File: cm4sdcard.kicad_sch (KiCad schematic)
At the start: 5 parts, among them J5 MEM2067-02-180-00-A_REVB, U9 LM3525M-H_NPOB

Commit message: respin
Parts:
- renumbered C18 to C20, C19 to C21, R24 to R27, U9 to U10
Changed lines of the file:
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@@
   (symbol (lib_id "power:GND") (at 178.435 128.27 0) (unit 1)
     (in_bom yes) (on_board yes)
-    (property "Reference" "#PWR030" (id 0) (at 178.435 134.62 0)
+    (property "Reference" "#PWR031" (id 0) (at 178.435 134.62 0)
       (effects (font (size 1.27 1.27)) hide)
     )
@@
   (symbol (lib_id "Device:R_Small") (at 104.14 66.04 90) (unit 1)
     (in_bom yes) (on_board yes) (fields_autoplaced)
-    (property "Reference" "R24" (id 0) (at 104.14 60.96 90))
+    (property "Reference" "R27" (id 0) (at 104.14 60.96 90))
     (property "Value" "12k 1%" (id 1) (at 104.14 63.5 90))
     (property "Footprint" "Resistor_SMD:R_0402_1005Metric" (id 2) (at 104.14 66.04 0)
@@
   (symbol (lib_id "Device:C_Small") (at 127 71.12 90) (unit 1)
     (in_bom yes) (on_board yes)
-    (property "Reference" "C18" (id 0) (at 125.73 69.85 90)
+    (property "Reference" "C20" (id 0) (at 125.73 69.85 90)
       (effects (font (size 1.27 1.27)) (justify left))
     )
@@
   (symbol (lib_id "power:GND") (at 167.64 83.82 0) (unit 1)
     (in_bom yes) (on_board yes)
-    (property "Reference" "#PWR029" (id 0) (at 167.64 90.17 0)
+    (property "Reference" "#PWR030" (id 0) (at 167.64 90.17 0)
       (effects (font (size 1.27 1.27)) hide)
     )
@@
   (symbol (lib_id "power:GND") (at 134.62 83.82 0) (unit 1)
     (in_bom yes) (on_board yes)
-    (property "Reference" "#PWR028" (id 0) (at 134.62 90.17 0)
+    (property "Reference" "#PWR029" (id 0) (at 134.62 90.17 0)
       (effects (font (size 1.27 1.27)) hide)
     )
@@
   (symbol (lib_id "Power_Protection_TI:LM3525M-H_NPOB") (at 144.78 68.58 0) (unit 1)
     (in_bom yes) (on_board yes)
-    (property "Reference" "U9" (id 0) (at 139.7 62.23 0))
+    (property "Reference" "U10" (id 0) (at 139.7 62.23 0))
     (property "Value" "LM3525M-H_NPOB" (id 1) (at 144.78 78.105 0))
     (property "Footprint" "Package_SO_MyOwn:SOIC-8_3.9x4.9mm_P1.27mm" (id 2) (at 145.034 86.106 0)
@@
   (symbol (lib_id "Device:C_Small") (at 167.64 68.58 0) (mirror x) (unit 1)
     (in_bom yes) (on_board yes)
-    (property "Reference" "C19" (id 0) (at 169.545 67.945 0)
+    (property "Reference" "C21" (id 0) (at 169.545 67.945 0)
       (effects (font (size 1.27 1.27)) (justify left))
     )

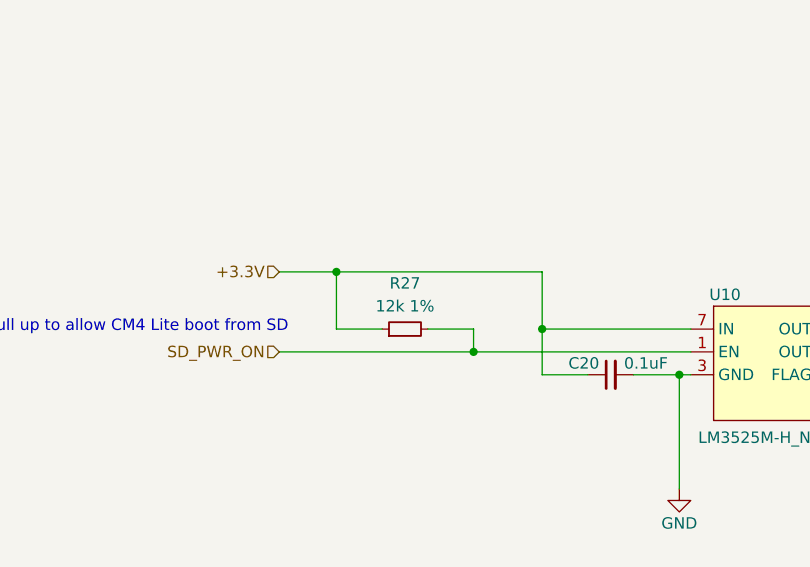
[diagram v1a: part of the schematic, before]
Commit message: fixed I2C ping indicator
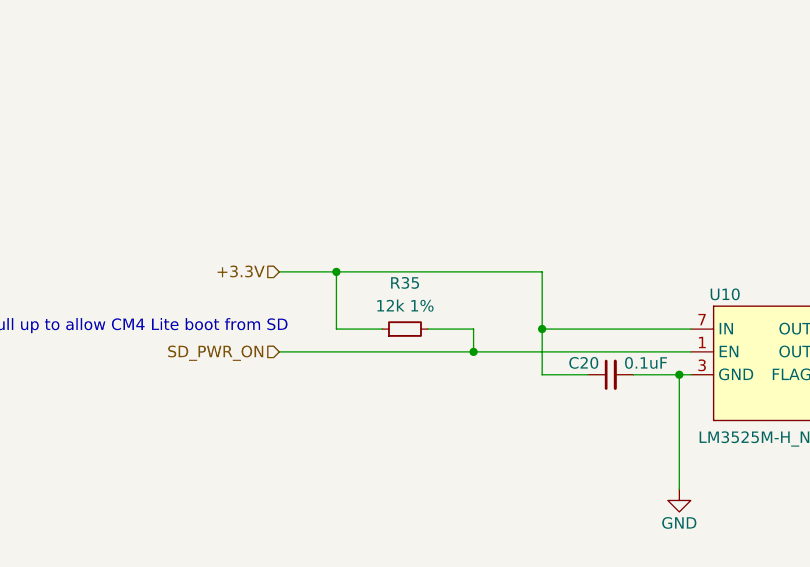
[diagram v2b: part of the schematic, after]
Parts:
- renumbered R27 to R35
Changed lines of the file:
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@@
   (symbol (lib_id "power:GND") (at 178.435 128.27 0) (unit 1)
     (in_bom yes) (on_board yes)
-    (property "Reference" "#PWR031" (id 0) (at 178.435 134.62 0)
+    (property "Reference" "#PWR033" (id 0) (at 178.435 134.62 0)
       (effects (font (size 1.27 1.27)) hide)
     )
@@
   (symbol (lib_id "Device:R_Small") (at 104.14 66.04 90) (unit 1)
     (in_bom yes) (on_board yes) (fields_autoplaced)
-    (property "Reference" "R27" (id 0) (at 104.14 60.96 90))
+    (property "Reference" "R35" (id 0) (at 104.14 60.96 90))
     (property "Value" "12k 1%" (id 1) (at 104.14 63.5 90))
     (property "Footprint" "Resistor_SMD:R_0402_1005Metric" (id 2) (at 104.14 66.04 0)
@@
   (symbol (lib_id "power:GND") (at 167.64 83.82 0) (unit 1)
     (in_bom yes) (on_board yes)
-    (property "Reference" "#PWR030" (id 0) (at 167.64 90.17 0)
+    (property "Reference" "#PWR032" (id 0) (at 167.64 90.17 0)
       (effects (font (size 1.27 1.27)) hide)
     )
@@
   (symbol (lib_id "power:GND") (at 134.62 83.82 0) (unit 1)
     (in_bom yes) (on_board yes)
-    (property "Reference" "#PWR029" (id 0) (at 134.62 90.17 0)
+    (property "Reference" "#PWR031" (id 0) (at 134.62 90.17 0)
       (effects (font (size 1.27 1.27)) hide)
     )

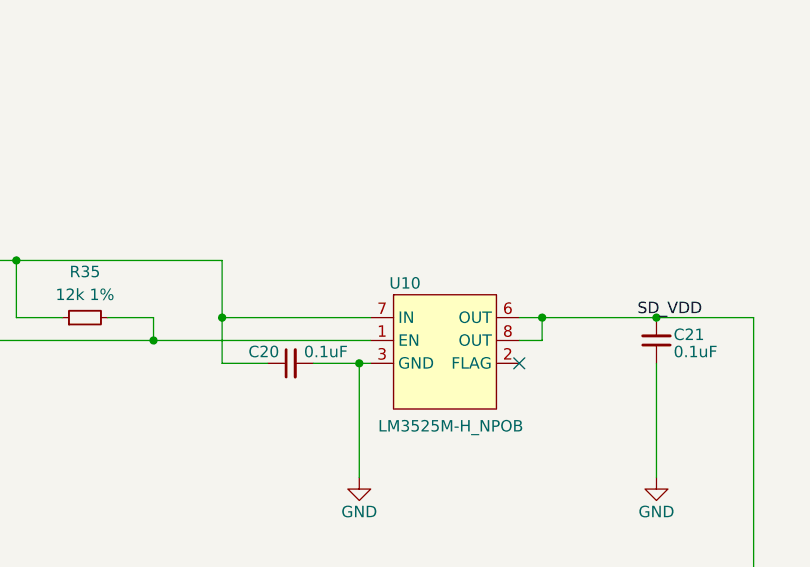
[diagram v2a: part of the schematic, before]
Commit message: added ti buffer lib
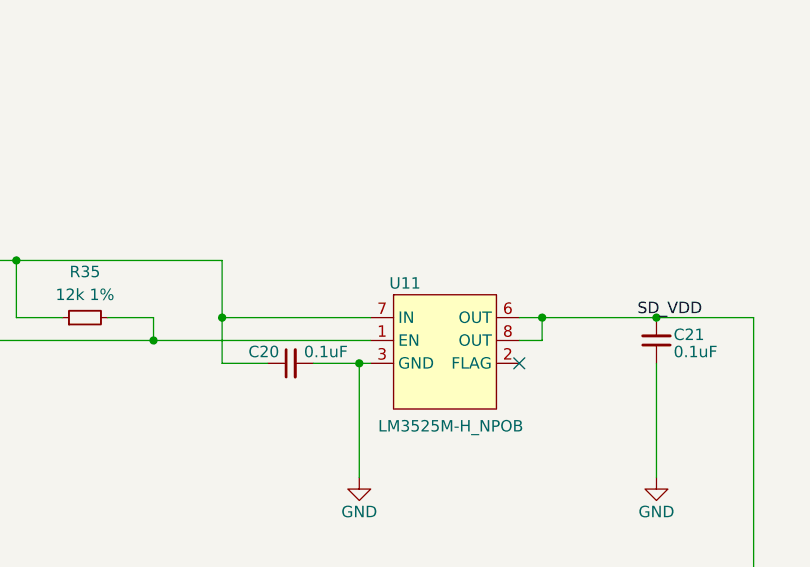
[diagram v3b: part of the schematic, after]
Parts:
- renumbered U10 to U11
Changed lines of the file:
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@@
   (symbol (lib_id "power:GND") (at 178.435 128.27 0) (unit 1)
     (in_bom yes) (on_board yes)
-    (property "Reference" "#PWR033" (id 0) (at 178.435 134.62 0)
+    (property "Reference" "#PWR035" (id 0) (at 178.435 134.62 0)
       (effects (font (size 1.27 1.27)) hide)
     )
@@
   (symbol (lib_id "power:GND") (at 167.64 83.82 0) (unit 1)
     (in_bom yes) (on_board yes)
-    (property "Reference" "#PWR032" (id 0) (at 167.64 90.17 0)
+    (property "Reference" "#PWR034" (id 0) (at 167.64 90.17 0)
       (effects (font (size 1.27 1.27)) hide)
     )
@@
   (symbol (lib_id "power:GND") (at 134.62 83.82 0) (unit 1)
     (in_bom yes) (on_board yes)
-    (property "Reference" "#PWR031" (id 0) (at 134.62 90.17 0)
+    (property "Reference" "#PWR033" (id 0) (at 134.62 90.17 0)
       (effects (font (size 1.27 1.27)) hide)
     )
@@
   (symbol (lib_id "Power_Protection_TI:LM3525M-H_NPOB") (at 144.78 68.58 0) (unit 1)
     (in_bom yes) (on_board yes)
-    (property "Reference" "U10" (id 0) (at 139.7 62.23 0))
+    (property "Reference" "U11" (id 0) (at 139.7 62.23 0))
     (property "Value" "LM3525M-H_NPOB" (id 1) (at 144.78 78.105 0))
     (property "Footprint" "Package_SO_MyOwn:SOIC-8_3.9x4.9mm_P1.27mm" (id 2) (at 145.034 86.106 0)

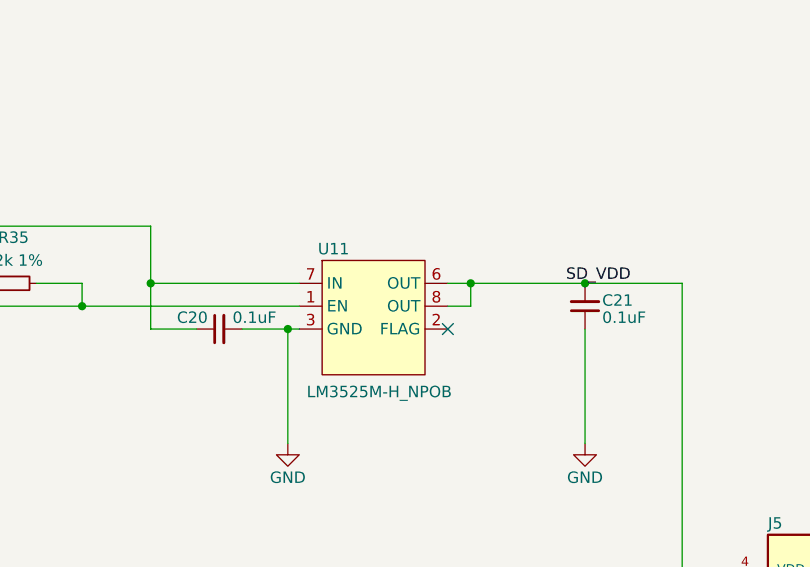
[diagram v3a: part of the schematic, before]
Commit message: initial integration of i2c arbiter
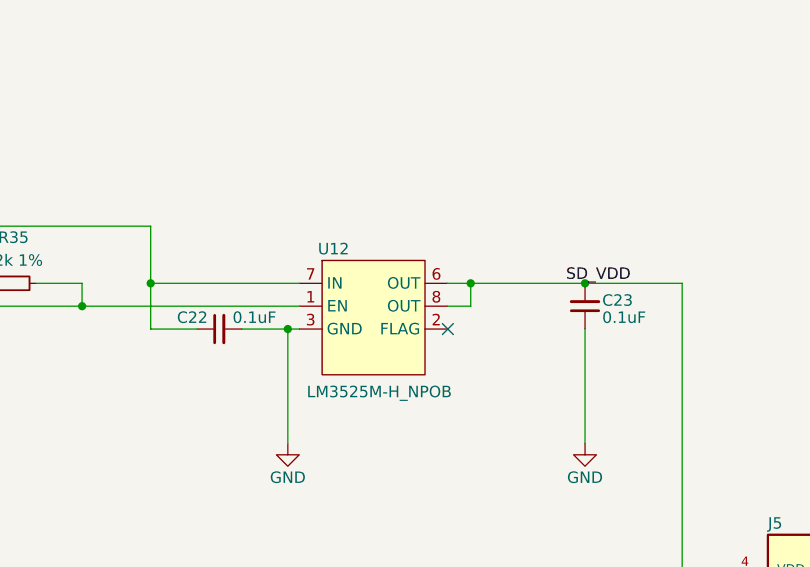
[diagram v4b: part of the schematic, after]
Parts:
- renumbered C20 to C22, C21 to C23, U11 to U12
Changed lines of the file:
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@@
   (symbol (lib_id "power:GND") (at 178.435 128.27 0) (unit 1)
     (in_bom yes) (on_board yes)
-    (property "Reference" "#PWR035" (id 0) (at 178.435 134.62 0)
+    (property "Reference" "#PWR036" (id 0) (at 178.435 134.62 0)
       (effects (font (size 1.27 1.27)) hide)
     )
@@
   (symbol (lib_id "Device:C_Small") (at 127 71.12 90) (unit 1)
     (in_bom yes) (on_board yes)
-    (property "Reference" "C20" (id 0) (at 125.73 69.85 90)
+    (property "Reference" "C22" (id 0) (at 125.73 69.85 90)
       (effects (font (size 1.27 1.27)) (justify left))
     )
@@
   (symbol (lib_id "power:GND") (at 167.64 83.82 0) (unit 1)
     (in_bom yes) (on_board yes)
-    (property "Reference" "#PWR034" (id 0) (at 167.64 90.17 0)
+    (property "Reference" "#PWR035" (id 0) (at 167.64 90.17 0)
       (effects (font (size 1.27 1.27)) hide)
     )
@@
   (symbol (lib_id "power:GND") (at 134.62 83.82 0) (unit 1)
     (in_bom yes) (on_board yes)
-    (property "Reference" "#PWR033" (id 0) (at 134.62 90.17 0)
+    (property "Reference" "#PWR034" (id 0) (at 134.62 90.17 0)
       (effects (font (size 1.27 1.27)) hide)
     )
@@
   (symbol (lib_id "Power_Protection_TI:LM3525M-H_NPOB") (at 144.78 68.58 0) (unit 1)
     (in_bom yes) (on_board yes)
-    (property "Reference" "U11" (id 0) (at 139.7 62.23 0))
+    (property "Reference" "U12" (id 0) (at 139.7 62.23 0))
     (property "Value" "LM3525M-H_NPOB" (id 1) (at 144.78 78.105 0))
     (property "Footprint" "Package_SO_MyOwn:SOIC-8_3.9x4.9mm_P1.27mm" (id 2) (at 145.034 86.106 0)
@@
   (symbol (lib_id "Device:C_Small") (at 167.64 68.58 0) (mirror x) (unit 1)
     (in_bom yes) (on_board yes)
-    (property "Reference" "C21" (id 0) (at 169.545 67.945 0)
+    (property "Reference" "C23" (id 0) (at 169.545 67.945 0)
       (effects (font (size 1.27 1.27)) (justify left))
     )

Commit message: footprint assignment
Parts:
- renumbered C22 to C24, C23 to C25, R35 to R41, U12 to U13
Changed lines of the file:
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@@
   (symbol (lib_id "power:GND") (at 178.435 128.27 0) (unit 1)
     (in_bom yes) (on_board yes)
-    (property "Reference" "#PWR036" (id 0) (at 178.435 134.62 0)
+    (property "Reference" "#PWR038" (id 0) (at 178.435 134.62 0)
       (effects (font (size 1.27 1.27)) hide)
     )
@@
   (symbol (lib_id "Device:R_Small") (at 104.14 66.04 90) (unit 1)
     (in_bom yes) (on_board yes) (fields_autoplaced)
-    (property "Reference" "R35" (id 0) (at 104.14 60.96 90))
+    (property "Reference" "R41" (id 0) (at 104.14 60.96 90))
     (property "Value" "12k 1%" (id 1) (at 104.14 63.5 90))
     (property "Footprint" "Resistor_SMD:R_0402_1005Metric" (id 2) (at 104.14 66.04 0)
@@
   (symbol (lib_id "Device:C_Small") (at 127 71.12 90) (unit 1)
     (in_bom yes) (on_board yes)
-    (property "Reference" "C22" (id 0) (at 125.73 69.85 90)
+    (property "Reference" "C24" (id 0) (at 125.73 69.85 90)
       (effects (font (size 1.27 1.27)) (justify left))
     )
@@
   (symbol (lib_id "power:GND") (at 167.64 83.82 0) (unit 1)
     (in_bom yes) (on_board yes)
-    (property "Reference" "#PWR035" (id 0) (at 167.64 90.17 0)
+    (property "Reference" "#PWR037" (id 0) (at 167.64 90.17 0)
       (effects (font (size 1.27 1.27)) hide)
     )
@@
   (symbol (lib_id "power:GND") (at 134.62 83.82 0) (unit 1)
     (in_bom yes) (on_board yes)
-    (property "Reference" "#PWR034" (id 0) (at 134.62 90.17 0)
+    (property "Reference" "#PWR036" (id 0) (at 134.62 90.17 0)
       (effects (font (size 1.27 1.27)) hide)
     )
@@
   (symbol (lib_id "Power_Protection_TI:LM3525M-H_NPOB") (at 144.78 68.58 0) (unit 1)
     (in_bom yes) (on_board yes)
-    (property "Reference" "U12" (id 0) (at 139.7 62.23 0))
+    (property "Reference" "U13" (id 0) (at 139.7 62.23 0))
     (property "Value" "LM3525M-H_NPOB" (id 1) (at 144.78 78.105 0))
     (property "Footprint" "Package_SO_MyOwn:SOIC-8_3.9x4.9mm_P1.27mm" (id 2) (at 145.034 86.106 0)
@@
   (symbol (lib_id "Device:C_Small") (at 167.64 68.58 0) (mirror x) (unit 1)
     (in_bom yes) (on_board yes)
-    (property "Reference" "C23" (id 0) (at 169.545 67.945 0)
+    (property "Reference" "C25" (id 0) (at 169.545 67.945 0)
       (effects (font (size 1.27 1.27)) (justify left))
     )
